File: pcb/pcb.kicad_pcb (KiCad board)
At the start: 6 copper layers, 194 parts, among them J1201 Conn_02x07_Top_Bottom, J1401 FPGA_JTAG, J201 USB_B_Mini, J301 Conn_02x05_Top_Bottom, J302 1658525-9, J601 DB15_Female_HighDensity, J801 10067847-001RLF, J901 FTSH-110-01-L-DV-007, U1402 S25FL127SABMFV101, U201 TPS54325PWPR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

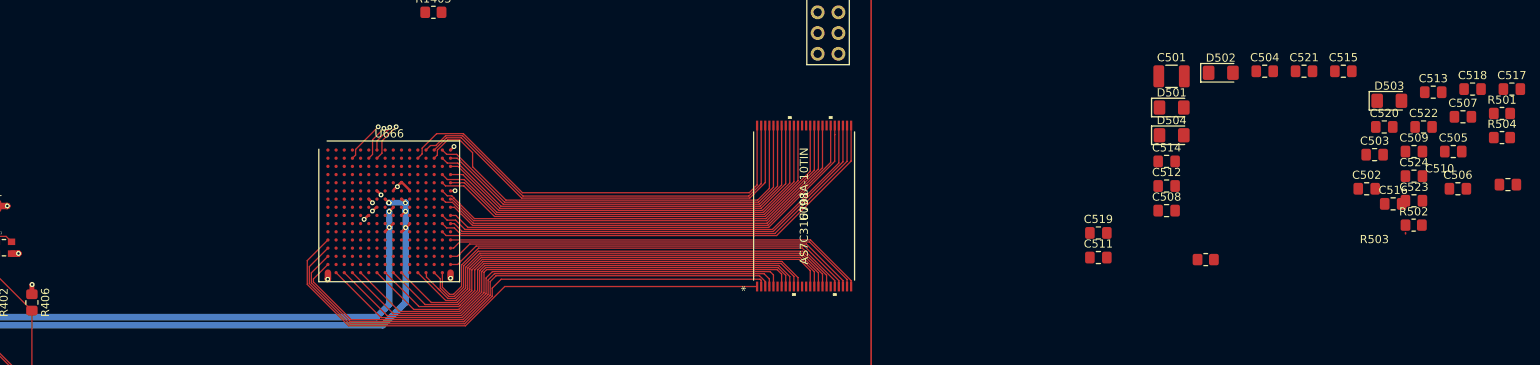
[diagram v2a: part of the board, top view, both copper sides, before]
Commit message: move capasitor
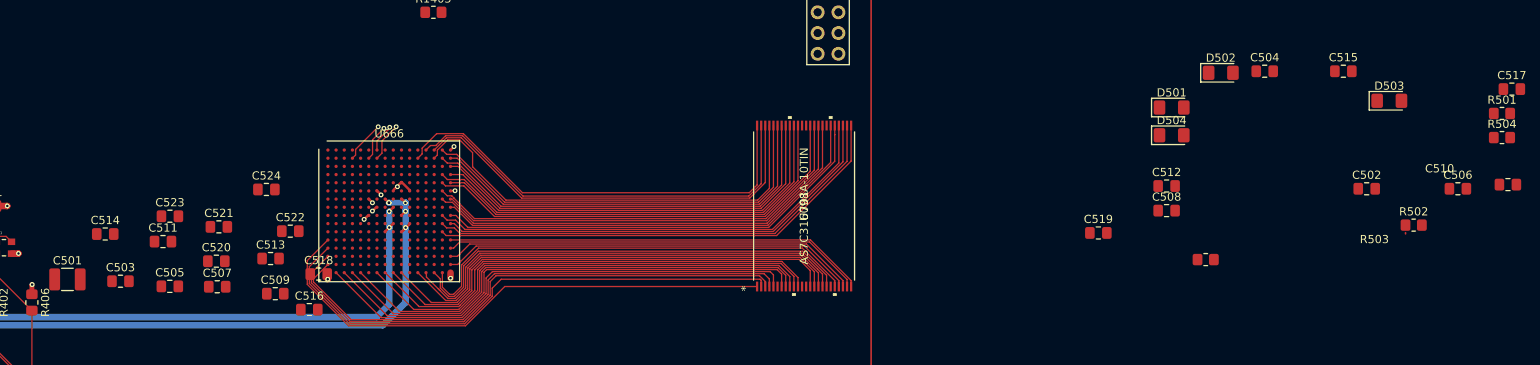
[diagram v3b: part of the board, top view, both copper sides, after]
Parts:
- moved C505 157.9 mm to (197.2, 108.5)
- moved C503 154.2 mm to (191.2, 107.9)
- moved C507 153.8 mm to (203.0, 108.6)
- moved C523 152.2 mm to (197.2, 100.0)
- moved C520 143.8 mm to (202.9, 105.5)
- moved C513 143.7 mm to (209.5, 105.1)
- moved C518 142.9 mm to (215.4, 107.0)
- moved C524 140.4 mm to (209.0, 96.7)
- moved C509 140.4 mm to (210.1, 109.4)
- moved C522 139.2 mm to (211.9, 101.8)
- moved C501 137.3 mm to (184.7, 107.7)
- moved C521 134.1 mm to (203.2, 101.2)
- moved C516 133.2 mm to (214.3, 111.4)
- moved C514 130.1 mm to (189.3, 102.1)
- moved C511 114.4 mm to (196.4, 103.0)
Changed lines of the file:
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@@
   )
   (footprint "Capacitor_SMD:C_0805_2012Metric_Pad1.18x1.45mm_HandSolder" (layer "F.Cu")
-    (at 349.402 95.046)
+    (at 209.025 96.675)
     (descr "Capacitor SMD 0805 (2012 Metric), square (rectangular) end terminal, IPC_7351 nominal with elongated pad for handsoldering. (Body size source: IPC-SM-782 page 76, https://www.pcb-3d.com/wordpress/wp-content/uploads/ipc-sm-782a_amendment_1_and_2.pdf, https://docs.google.com/spreadsheets/d/1BsfQQcO9C6DZCsRaXUlFlo91Tg2WpOkGARC1WS5S8t0/edit?usp=sharing), generated with kicad-footprint-generator")
     (tags "capacitor handsolder")
@@
   )
   (footprint "Capacitor_SMD:C_0805_2012Metric_Pad1.18x1.45mm_HandSolder" (layer "F.Cu")
-    (at 356.572 84.396)
+    (at 215.425 107.025)
     (descr "Capacitor SMD 0805 (2012 Metric), square (rectangular) end terminal, IPC_7351 nominal with elongated pad for handsoldering. (Body size source: IPC-SM-782 page 76, https://www.pcb-3d.com/wordpress/wp-content/uploads/ipc-sm-782a_amendment_1_and_2.pdf, https://docs.google.com/spreadsheets/d/1BsfQQcO9C6DZCsRaXUlFlo91Tg2WpOkGARC1WS5S8t0/edit?usp=sharing), generated with kicad-footprint-generator")
     (tags "capacitor handsolder")
@@
   )
   (footprint "Capacitor_SMD:C_0805_2012Metric_Pad1.18x1.45mm_HandSolder" (layer "F.Cu")
-    (at 349.402 98.056)
+    (at 197.225 99.95)
     (descr "Capacitor SMD 0805 (2012 Metric), square (rectangular) end terminal, IPC_7351 nominal with elongated pad for handsoldering. (Body size source: IPC-SM-782 page 76, https://www.pcb-3d.com/wordpress/wp-content/uploads/ipc-sm-782a_amendment_1_and_2.pdf, https://docs.google.com/spreadsheets/d/1BsfQQcO9C6DZCsRaXUlFlo91Tg2WpOkGARC1WS5S8t0/edit?usp=sharing), generated with kicad-footprint-generator")
     (tags "capacitor handsolder")
@@
   )
   (footprint "Capacitor_SMD:C_0805_2012Metric_Pad1.18x1.45mm_HandSolder" (layer "F.Cu")
-    (at 350.582 89.026)
+    (at 211.95 101.775)
     (descr "Capacitor SMD 0805 (2012 Metric), square (rectangular) end terminal, IPC_7351 nominal with elongated pad for handsoldering. (Body size source: IPC-SM-782 page 76, https://www.pcb-3d.com/wordpress/wp-content/uploads/ipc-sm-782a_amendment_1_and_2.pdf, https://docs.google.com/spreadsheets/d/1BsfQQcO9C6DZCsRaXUlFlo91Tg2WpOkGARC1WS5S8t0/edit?usp=sharing), generated with kicad-footprint-generator")
     (tags "capacitor handsolder")
@@
   )
   (footprint "Capacitor_SMD:C_0805_2012Metric_Pad1.18x1.45mm_HandSolder" (layer "F.Cu")
-    (at 335.958 82.212)
+    (at 203.2125 101.25)
     (descr "Capacitor SMD 0805 (2012 Metric), square (rectangular) end terminal, IPC_7351 nominal with elongated pad for handsoldering. (Body size source: IPC-SM-782 page 76, https://www.pcb-3d.com/wordpress/wp-content/uploads/ipc-sm-782a_amendment_1_and_2.pdf, https://docs.google.com/spreadsheets/d/1BsfQQcO9C6DZCsRaXUlFlo91Tg2WpOkGARC1WS5S8t0/edit?usp=sharing), generated with kicad-footprint-generator")
     (tags "capacitor handsolder")
@@
       (effects (font (size 1 1) (thickness 0.15)))
     )
-    (fp_text value "470n" (at 20.634 0.854) (layer "F.Fab")
+    (fp_text value "470n" (at -0.025 0.1) (layer "F.Fab")
       (effects (font (size 1 1) (thickness 0.15)))
     )
@@
   )
   (footprint "Capacitor_SMD:C_0805_2012Metric_Pad1.18x1.45mm_HandSolder" (layer "F.Cu")
-    (at 354.212 92.036)
+    (at 197.2125 108.525)
     (descr "Capacitor SMD 0805 (2012 Metric), square (rectangular) end terminal, IPC_7351 nominal with elongated pad for handsoldering. (Body size source: IPC-SM-782 page 76, https://www.pcb-3d.com/wordpress/wp-content/uploads/ipc-sm-782a_amendment_1_and_2.pdf, https://docs.google.com/spreadsheets/d/1BsfQQcO9C6DZCsRaXUlFlo91Tg2WpOkGARC1WS5S8t0/edit?usp=sharing), generated with kicad-footprint-generator")
     (tags "capacitor handsolder")
@@
   )
   (footprint "Capacitor_SMD:C_0805_2012Metric_Pad1.18x1.45mm_HandSolder" (layer "F.Cu")
-    (at 319.148 93.242)
+    (at 189.3125 102.125)
     (descr "Capacitor SMD 0805 (2012 Metric), square (rectangular) end terminal, IPC_7351 nominal with elongated pad for handsoldering. (Body size source: IPC-SM-782 page 76, https://www.pcb-3d.com/wordpress/wp-content/uploads/ipc-sm-782a_amendment_1_and_2.pdf, https://docs.google.com/spreadsheets/d/1BsfQQcO9C6DZCsRaXUlFlo91Tg2WpOkGARC1WS5S8t0/edit?usp=sharing), generated with kicad-footprint-generator")
     (tags "capacitor handsolder")
@@
   )
   (footprint "Capacitor_SMD:C_0805_2012Metric_Pad1.18x1.45mm_HandSolder" (layer "F.Cu")
-    (at 349.402 92.036)
+    (at 210.1125 109.425)
     (descr "Capacitor SMD 0805 (2012 Metric), square (rectangular) end terminal, IPC_7351 nominal with elongated pad for handsoldering. (Body size source: IPC-SM-782 page 76, https://www.pcb-3d.com/wordpress/wp-content/uploads/ipc-sm-782a_amendment_1_and_2.pdf, https://docs.google.com/spreadsheets/d/1BsfQQcO9C6DZCsRaXUlFlo91Tg2WpOkGARC1WS5S8t0/edit?usp=sharing), generated with kicad-footprint-generator")
     (tags "capacitor handsolder")
@@
   )
   (footprint "Capacitor_SMD:C_0805_2012Metric_Pad1.18x1.45mm_HandSolder" (layer "F.Cu")
-    (at 351.762 84.776)
+    (at 209.5375 105.125)
     (descr "Capacitor SMD 0805 (2012 Metric), square (rectangular) end terminal, IPC_7351 nominal with elongated pad for handsoldering. (Body size source: IPC-SM-782 page 76, https://www.pcb-3d.com/wordpress/wp-content/uploads/ipc-sm-782a_amendment_1_and_2.pdf, https://docs.google.com/spreadsheets/d/1BsfQQcO9C6DZCsRaXUlFlo91Tg2WpOkGARC1WS5S8t0/edit?usp=sharing), generated with kicad-footprint-generator")
     (tags "capacitor handsolder")
@@
   )
   (footprint "Capacitor_SMD:C_0805_2012Metric_Pad1.18x1.45mm_HandSolder" (layer "F.Cu")
-    (at 346.862 98.436)
+    (at 214.275 111.375)
     (descr "Capacitor SMD 0805 (2012 Metric), square (rectangular) end terminal, IPC_7351 nominal with elongated pad for handsoldering. (Body size source: IPC-SM-782 page 76, https://www.pcb-3d.com/wordpress/wp-content/uploads/ipc-sm-782a_amendment_1_and_2.pdf, https://docs.google.com/spreadsheets/d/1BsfQQcO9C6DZCsRaXUlFlo91Tg2WpOkGARC1WS5S8t0/edit?usp=sharing), generated with kicad-footprint-generator")
     (tags "capacitor handsolder")
@@
   )
   (footprint "Capacitor_SMD:C_1210_3225Metric_Pad1.33x2.70mm_HandSolder" (layer "F.Cu")
-    (at 319.748 82.832)
+    (at 184.6875 107.675)
     (descr "Capacitor SMD 1210 (3225 Metric), square (rectangular) end terminal, IPC_7351 nominal with elongated pad for handsoldering. (Body size source: IPC-SM-782 page 76, https://www.pcb-3d.com/wordpress/wp-content/uploads/ipc-sm-782a_amendment_1_and_2.pdf), generated with kicad-footprint-generator")
     (tags "capacitor handsolder")
@@
   )
   (footprint "Capacitor_SMD:C_0805_2012Metric_Pad1.18x1.45mm_HandSolder" (layer "F.Cu")
-    (at 310.798 105.002)
+    (at 196.375 103.05)
     (descr "Capacitor SMD 0805 (2012 Metric), square (rectangular) end terminal, IPC_7351 nominal with elongated pad for handsoldering. (Body size source: IPC-SM-782 page 76, https://www.pcb-3d.com/wordpress/wp-content/uploads/ipc-sm-782a_amendment_1_and_2.pdf, https://docs.google.com/spreadsheets/d/1BsfQQcO9C6DZCsRaXUlFlo91Tg2WpOkGARC1WS5S8t0/edit?usp=sharing), generated with kicad-footprint-generator")
     (tags "capacitor handsolder")
@@
   )
   (footprint "Capacitor_SMD:C_0805_2012Metric_Pad1.18x1.45mm_HandSolder" (layer "F.Cu")
-    (at 355.392 87.786)
+    (at 203.0125 108.575)
     (descr "Capacitor SMD 0805 (2012 Metric), square (rectangular) end terminal, IPC_7351 nominal with elongated pad for handsoldering. (Body size source: IPC-SM-782 page 76, https://www.pcb-3d.com/wordpress/wp-content/uploads/ipc-sm-782a_amendment_1_and_2.pdf, https://docs.google.com/spreadsheets/d/1BsfQQcO9C6DZCsRaXUlFlo91Tg2WpOkGARC1WS5S8t0/edit?usp=sharing), generated with kicad-footprint-generator")
     (tags "capacitor handsolder")
@@
   )
   (footprint "Capacitor_SMD:C_0805_2012Metric_Pad1.18x1.45mm_HandSolder" (layer "F.Cu")
-    (at 344.592 92.416)
+    (at 191.175 107.9)
     (descr "Capacitor SMD 0805 (2012 Metric), square (rectangular) end terminal, IPC_7351 nominal with elongated pad for handsoldering. (Body size source: IPC-SM-782 page 76, https://www.pcb-3d.com/wordpress/wp-content/uploads/ipc-sm-782a_amendment_1_and_2.pdf, https://docs.google.com/spreadsheets/d/1BsfQQcO9C6DZCsRaXUlFlo91Tg2WpOkGARC1WS5S8t0/edit?usp=sharing), generated with kicad-footprint-generator")
     (tags "capacitor handsolder")
@@
   )
   (footprint "Capacitor_SMD:C_0805_2012Metric_Pad1.18x1.45mm_HandSolder" (layer "F.Cu")
-    (at 345.772 89.026)
+    (at 202.9 105.45)
     (descr "Capacitor SMD 0805 (2012 Metric), square (rectangular) end terminal, IPC_7351 nominal with elongated pad for handsoldering. (Body size source: IPC-SM-782 page 76, https://www.pcb-3d.com/wordpress/wp-content/uploads/ipc-sm-782a_amendment_1_and_2.pdf, https://docs.google.com/spreadsheets/d/1BsfQQcO9C6DZCsRaXUlFlo91Tg2WpOkGARC1WS5S8t0/edit?usp=sharing), generated with kicad-footprint-generator")
     (tags "capacitor handsolder")
@@
       (pts
         (xy 227.076 102.362)
-        (xy 220.98 102.362)
-        (xy 220.98 95.25)
+        (xy 188.8 106.675)
+        (xy 186.925 95.25)
         (xy 227.076 95.25)
       )

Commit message: add 1.0v and 1.8v decoupling for fpga, clean capacitors
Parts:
- moved C1105 266.3 mm to (143.3, -60.5), turned to 90 degrees
- moved C1108 262.4 mm to (152.7, -66.1), turned to 90 degrees
- moved C1109 260.8 mm to (152.7, -60.4), turned to 90 degrees
- moved C1110 259.3 mm to (156.7, -66.3), turned to 90 degrees
- moved C1112 259.3 mm to (160.8, -66.3), turned to 90 degrees
- moved C1111 258.4 mm to (156.7, -60.4), turned to 90 degrees
- moved C517 160.7 mm to (202.8, 110.7)
- moved C515 147.7 mm to (195.9, 110.7)
- moved C1115 134.5 mm to (164.8, -60.4), turned to 90 degrees
- moved C506 134.0 mm to (222.5, 117.9), turned to 90 degrees
- moved C510 133.1 mm to (229.6, 117.9), turned to 90 degrees
- moved C1113 130.1 mm to (160.8, -60.4), turned to 90 degrees
- moved C502 129.7 mm to (215.6, 117.9), turned to 90 degrees
- moved C1114 129.3 mm to (164.8, -66.3), turned to 90 degrees
- moved Y1101 118.2 mm to (146.1, -78.1)
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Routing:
- net GND: track 141.9 -> 177.0 mm, vias 44 -> 70
- net +1V0: track 196.2 -> 223.4 mm, vias 7 -> 25
- net +1V8: track 202.5 -> 210.3 mm, vias 6 -> 13
- net +3.3V: track 34.2 -> 37.7 mm, vias 21 -> 23
- net FGPA_MCU_SPI_CS: track 88.2 -> 89.2 mm
- added copper zone on In3.Cu, net +1V8
- removed copper zone on In1.Cu, net +1V0

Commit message: vga is live
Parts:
- removed the R601 at (151.0, 62.0)
- removed the R602 at (154.2, 62.1)
- removed the R603 at (156.2, 62.1)
- removed the R604 at (159.6, 62.0)
- removed the R605 at (162.4, 62.2)
- removed the R606 at (164.8, 55.1)
- removed the R607 at (168.1, 55.1)
- removed the R608 at (171.1, 55.1)
- removed the R609 at (174.1, 55.1)
- removed the R610 at (176.1, 55.1)
- removed the R611 at (178.0, 55.1)
- removed the R612 at (178.1, 62.9)
- removed the R613 at (181.5, 62.9)
- removed the R614 at (184.5, 62.8)
- removed the R615 at (187.2, 62.9)
- removed the R616 at (190.3, 62.8)
- moved C1101 214.2 mm to (242.2, 114.8), turned to 90 degrees
- moved Y1101 214.0 mm to (238.8, 114.8), turned to 90 degrees
- moved R609 134.5 mm to (177.5, 53.5), turned to 90 degrees
- moved R610 131.9 mm to (174.5, 53.5), turned to 90 degrees
- moved R611 127.5 mm to (171.5, 53.5), turned to 90 degrees
- moved R608 123.0 mm to (180.0, 53.5), turned to 90 degrees
- moved R607 122.2 mm to (183.0, 53.5), turned to 90 degrees
- moved R606 121.8 mm to (186.0, 53.5), turned to 90 degrees
- moved R614 119.0 mm to (201.5, 53.5), turned to 90 degrees
- moved R616 116.4 mm to (195.5, 53.5), turned to 90 degrees
- moved R615 112.6 mm to (198.5, 53.5), turned to 90 degrees
- moved R612 112.4 mm to (207.5, 53.5), turned to 90 degrees
- moved R613 112.3 mm to (204.5, 53.5), turned to 90 degrees
- moved C1102 52.3 mm to (163.2, -20.7)
- moved C1103 52.3 mm to (163.2, -14.6)
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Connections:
- U666 pad A10: vga_g1 -> vga_b2
- U666 pad A12: vga_g5 -> vga_hsync
- U666 pad A2: /fpga/fpga ub/FPGA_GPIO_9 -> vga_r2
- U666 pad A3: /fpga/fpga ub/FPGA_GPIO_1 -> vga_r4
- U666 pad A4: unconnected-(U666-PadA4) -> vga_r5
- U666 pad A5: FGPA_MCU_EXTRA2 -> vga_g5
- U666 pad A7: FGPA_MCU_SPI_SDI -> vga_g2
- U666 pad A8: vga_b3 -> vga_b5
- U666 pad B1: /fpga/fpga ub/FPGA_GPIO_11 -> vga_r1
- U666 pad B10: vga_g2 -> vga_b1
- U666 pad B11: vga_g3 -> vga_vsync
- U666 pad B2: /fpga/fpga ub/FPGA_GPIO_8 -> vga_r3
- U666 pad B4: FGPA_MCU_SPI_CLK -> vga_g6
- U666 pad B5: FGPA_MCU_EXTRA1 -> vga_g4
- U666 pad B6: FGPA_MCU_SPI_SDO -> vga_g3
- U666 pad B7: FGPA_MCU_SPI_CS -> vga_g1
- U666 pad B9: vga_b5 -> vga_b3
- U666 pad C1: /fpga/fpga ub/FPGA_GPIO_10 -> unconnected-(U666-PadC1)
- U666 pad C14: vga_r4 -> /fpga/fpga ua/FPGA_GPIO_1
- U666 pad C2: /fpga/fpga ub/FPGA_GPIO_7 -> unconnected-(U666-PadC2)
- U666 pad C8: vga_b1 -> /fpga/fpga ua/FPGA_GPIO_7
- U666 pad C9: vga_b2 -> /fpga/fpga ua/FPGA_GPIO_10
- U666 pad D8: vga_g6 -> /fpga/fpga ua/FPGA_GPIO_8
- U666 pad D9: vga_r1 -> unconnected-(U666-PadD9)
- U666 pad F2: unconnected-(U666-PadF2) -> FGPA_MCU_EXTRA1
- U666 pad G1: unconnected-(U666-PadG1) -> FGPA_MCU_SPI_CS
- U666 pad G2: unconnected-(U666-PadG2) -> FGPA_MCU_SPI_SDI
- U666 pad H1: unconnected-(U666-PadH1) -> FGPA_MCU_SPI_SDO
- U666 pad H2: unconnected-(U666-PadH2) -> FGPA_MCU_SPI_CLK
- U666 pad J13: vga_r5 -> unconnected-(U666-PadJ13)
- U666 pad L14: vga_r2 -> /fpga/fpga ua/FPGA_GPIO_9
- U666 pad M14: vga_r3 -> unconnected-(U666-PadM14)
- U666 pad M15: vga_g4 -> unconnected-(U666-PadM15)
- U666 pad N11: FPGA_OSCILLATOR_CLOCK -> unconnected-(U666-PadN11)
- U666 pad N14: vga_hsync -> unconnected-(U666-PadN14)
- U666 pad P14: unconnected-(U666-PadP14) -> FPGA_OSCILLATOR_CLOCK
- U666 pad P9: vga_vsync -> /fpga/fpga ua/FPGA_GPIO_11
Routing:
- net vga_r1: track 0.00 -> 112.8 mm
- net vga_r2: track 0.00 -> 108.7 mm
- net vga_r3: track 0.00 -> 107.1 mm
- net vga_r4: track 0.00 -> 103.2 mm
- net vga_r5: track 0.00 -> 100.8 mm
- net vga_g6: track 0.00 -> 92.7 mm
- net vga_g5: track 0.00 -> 86.5 mm
- net vga_g4: track 0.00 -> 85.5 mm
- net vga_g3: track 0.00 -> 82.7 mm
- net vga_g2: track 0.00 -> 78.8 mm
- net vga_g1: track 0.00 -> 77.2 mm
- net FGPA_MCU_EXTRA1: track 0.00 -> 74.3 mm, vias 0 -> 4
- net vga_b5: track 0.00 -> 69.6 mm
- net vga_b4: track 0.00 -> 63.7 mm
- net vga_b3: track 0.00 -> 62.2 mm
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
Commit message: decouple fpga, clean up a bit
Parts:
- moved D504 163.0 mm to (193.3, 154.9)
- moved R504 161.9 mm to (193.0, 149.9)
- moved D501 158.1 mm to (198.6, 154.9)
- moved R501 150.8 mm to (198.0, 149.9)
- moved R502 145.4 mm to (203.7, 149.9)
- moved D502 145.1 mm to (204.1, 154.9)
- moved D503 141.9 mm to (209.6, 154.9)
- moved R503 133.3 mm to (209.1, 149.9)
- moved C1103 132.2 mm to (244.1, 89.9)
- moved C1105 132.2 mm to (249.8, 89.7)
- moved C1107 132.2 mm to (254.3, 89.7)
- moved J801 128.9 mm to (134.6, 33.0)
- moved C801 127.9 mm to (128.0, 77.4)
- moved C802 127.9 mm to (128.3, 65.8)
- moved R804 127.9 mm to (133.0, 68.8)
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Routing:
- net +3.3V: track 52.1 -> 91.4 mm, vias 36 -> 66
- net GND: track 176.6 -> 212.1 mm, vias 90 -> 117
